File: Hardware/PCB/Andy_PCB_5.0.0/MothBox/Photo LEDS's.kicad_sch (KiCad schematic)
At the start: 48 parts, among them Q4 TJ10S04M3L,LXHQ, Q5 TJ10S04M3L,LXHQ, Q6 BC817, Q7 BC817

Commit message: made better camera
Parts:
- renumbered D1 to D10, D2 to D11, D3 to D12, D4 to D13, D5 to D14, D6 to D15, D7 to D16, D8 to D17, D9 to D18, D10 to D19, D11 to D20, D12 to D21, D13 to D22, D14 to D23, D15 to D24, D16 to D25, D17 to D26, D18 to D27, D19 to D28, D20 to D29, Q6 to Q4, Q4 to Q5, Q7 to Q6, Q5 to Q7, R55 to R51, R56 to R52, R57 to R53, R53 to R54, R58 to R55, R59 to R56, R51 to R57, R60 to R58, R61 to R59, R62 to R60, R63 to R61, R64 to R62, R65 to R63, R66 to R64, R67 to R65, R54 to R66, R68 to R67, R69 to R68, R52 to R69

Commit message: added female inverted header
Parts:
- removed D10, D11, D13, D14, D15, D16, D17, D18, D19, D20, D21, D22, D23, D24, D25, D26, D27, D28, D29: LED, LED_SMD:LED_Everlight-SMD3528_3.5x2.8mm_67-21ST, symbol Device:LED
- removed R52, R53, R55, R56, R58, R59, R60, R61, R62, R63, R64, R65, R67, R68, R70, R71, R72, R73, R74: 170R, Resistor_SMD:R_2512_6332Metric, symbol Device:R_US
- added LED1, LED10, LED11, LED13, LED14, LED15, LED16, LED17, LED18, LED19, LED2, LED20, LED21, LED22, LED23, LED24, LED25, LED26, LED27, LED28, LED29, LED3, LED34, LED35, LED36, LED37, LED38, LED39, LED4, LED40, LED41, LED42, LED43, LED44, LED45, LED46, LED47, LED48, LED49, LED5, LED50, LED51, LED52, LED6, LED7, LED8, LED9: XL-2835UWC-02, easyeda2kicad:LED-SMD_L3.5-W2.8-RD_1.25T-2PWT, symbol easyeda2kicad:XL-2835UWC-02
- added R10, R11, R12, R13, R14, R15, R2, R3, R52, R53, R55, R6, R7, R8, R9: FRC0805F30R0TS, easyeda2kicad:R0805, symbol easyeda2kicad:FRC0805F30R0TS
- LED12: renamed from D12; value LED -> XL-2835UWC-02; footprint LED_SMD:LED_Everlight-SMD3528_3.5x2.8mm_67-21ST -> easyeda2kicad:LED-SMD_L3.5-W2.8-RD_1.25T-2PWT; symbol Device:LED -> easyeda2kicad:XL-2835UWC-02; LCSC Part (none) -> C2843876
- R51: value 170R -> FRC0805F30R0TS; footprint Resistor_SMD:R_2512_6332Metric -> easyeda2kicad:R0805; symbol Device:R_US -> easyeda2kicad:FRC0805F30R0TS; LCSC Part (none) -> C2907256
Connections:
- net +12V_L_LED: now also R51.2, R2.2, R3.2, R53.2, R6.2, R7.2, R8.2, R9.2; no longer R51.1
- net +12V_R_LED: now also R10.2, R11.2, R12.2, R13.2, R14.2, R15.2, R52.2, R55.2
- net GND: now also LED11.1 (K), LED15.1 (K), LED18.1 (K), LED2.1 (K), LED22.1 (K), LED25.1 (K), LED28.1 (K), LED35.1 (K), LED37.1 (K), LED40.1 (K), LED43.1 (K), LED46.1 (K), LED49.1 (K), LED5.1 (K), LED52.1 (K), LED8.1 (K); no longer LED12.1 (K)
- net at LED12.2 (A): now also R51.1
- new net: LED6.2 (A), R3.1
- new net: LED16.1 (K), LED17.2 (A)
- new net: LED16.2 (A), R8.1
- new net: LED14.1 (K), LED15.2 (A)
- new net: LED23.2 (A), R11.1
- new net: LED42.1 (K), LED43.2 (A)
- new net: LED41.1 (K), LED42.2 (A)
- new net: LED45.1 (K), LED46.2 (A)
- new net: LED44.1 (K), LED45.2 (A)
- new net: LED9.2 (A), R6.1
- new net: LED7.1 (K), LED8.2 (A)
- new net: LED4.1 (K), LED5.2 (A)
- new net: LED21.1 (K), LED22.2 (A)
- new net: LED20.1 (K), LED21.2 (A)
- new net: LED19.2 (A), R9.1
- new net: LED48.1 (K), LED49.2 (A)
- new net: LED47.1 (K), LED48.2 (A)
- new net: LED29.1 (K), LED36.2 (A)
- new net: LED29.2 (A), R13.1
- new net: LED20.2 (A), R10.1
- new net: LED27.1 (K), LED28.2 (A)
- new net: LED34.1 (K), LED35.2 (A)
- new net: LED19.1 (K), LED34.2 (A)
- new net: LED50.1 (K), LED51.2 (A)
- new net: LED50.2 (A), R55.1
- new net: LED10.1 (K), LED11.2 (A)
- new net: LED10.2 (A), LED9.1 (K)
- new net: LED1.1 (K), LED2.2 (A)
- new net: LED1.2 (A), LED12.1 (K)
- new net: LED13.1 (K), LED14.2 (A)
- new net: LED13.2 (A), R7.1
- new net: LED36.1 (K), LED37.2 (A)
- new net: LED44.2 (A), R52.1
- new net: LED38.1 (K), LED39.2 (A)
- new net: LED38.2 (A), R14.1
- new net: LED39.1 (K), LED40.2 (A)
- new net: LED17.1 (K), LED18.2 (A)
- new net: LED26.1 (K), LED27.2 (A)
- new net: LED26.2 (A), R12.1
- new net: LED51.1 (K), LED52.2 (A)
- new net: LED3.1 (K), LED4.2 (A)
- new net: LED3.2 (A), R2.1
- new net: LED6.1 (K), LED7.2 (A)
- new net: LED41.2 (A), R15.1
- new net: LED23.1 (K), LED24.2 (A)
- new net: LED24.1 (K), LED25.2 (A)
- new net: LED47.2 (A), R53.1
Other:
- note added: "XINGLIGHT XL-2835UWC-02 60mA 6000K~7500K Yellow lens -20℃~+85℃ Positive Stick White 120° 200mW 3.4V SMD2835 LED Indication - Discrete ROH Figure out: How much current do these LEDs need how many batches per transistor thing what is the light angle of these LEDS (if any) without lens is cheaper Current per led = 60mA Total current = 8(columns) x 60mA = 480mA Total Luminous required = ?? lm Per led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"
- note removed: "Current per led = 55mA Total current = 10 x 55mA = 550mA Total Luminous required = 274 lm Per led luminous = 34 lm 10 led Luminous = 340 lm"

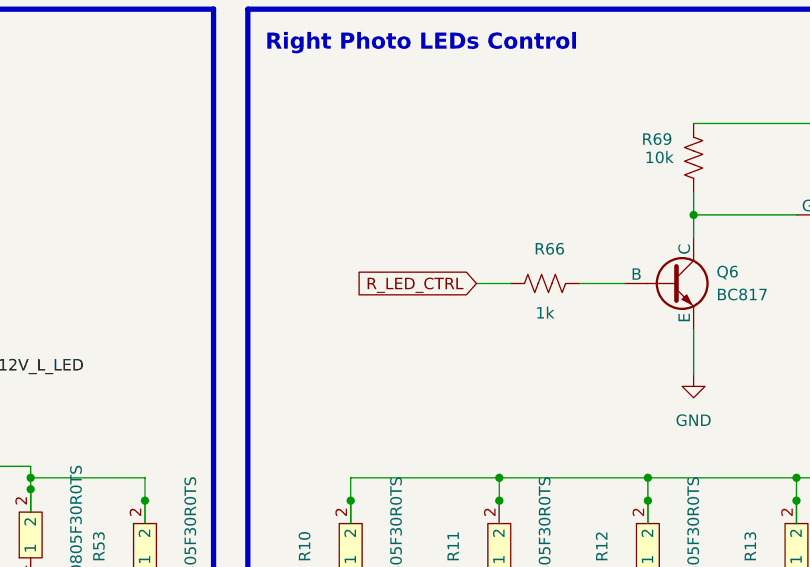
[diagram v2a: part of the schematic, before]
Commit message: Almost everything wired up
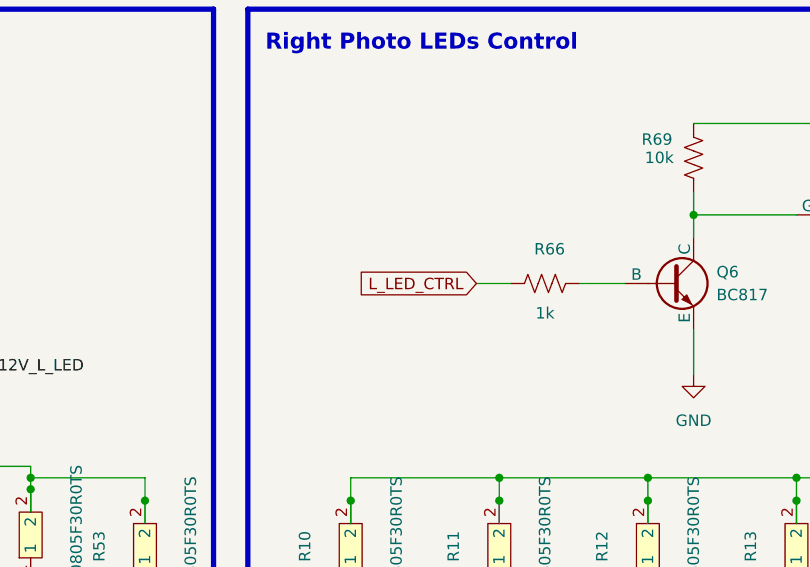
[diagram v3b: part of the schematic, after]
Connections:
- net R_LED_CTRL is gone; now on net L_LED_CTRL: R66.2
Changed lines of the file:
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@@
 		)
 	)
-	(global_label "R_LED_CTRL"
+	(global_label "L_LED_CTRL"
 		(shape input)
 		(at 179.07 66.04 180)
@@
 		)
 		(property "Intersheetrefs" "${INTERSHEET_REFS}"
-			(at 164.8968 66.04 0)
+			(at 165.1387 66.04 0)
 			(effects
 				(font

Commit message: omg pretty much all wired
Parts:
- added TP5: +12VLED L, TestPoint:TestPoint_THTPad_D1.0mm_Drill0.5mm, symbol Connector:TestPoint
- added TP6: +12VLED R, TestPoint:TestPoint_THTPad_D1.0mm_Drill0.5mm, symbol Connector:TestPoint
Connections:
- net +12V_L_LED: now also TP5.1
- net +12V_R_LED: now also TP6.1
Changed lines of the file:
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@@
 	)
 	(junction
+		(at 95.25 86.36)
+		(diameter 0)
+		(color 0 0 0 0)
+	)
+	(junction
 		(at 85.09 55.88)
 		(diameter 0)
@@
 		(color 0 0 0 0)
 	)
+	(junction
+		(at 223.52 87.63)
+		(diameter 0)
+		(color 0 0 0 0)
+	)
 	(wire
 		(pts
@@
 	(wire
 		(pts
+			(xy 223.52 87.63) (xy 229.87 87.63)
+		)
+		(stroke
+			(width 0)
+			(type default)
+		)
+	)
+	(wire
+		(pts
 			(xy 105.41 149.86) (xy 113.03 149.86)
 		)
@@
 	(wire
 		(pts
+			(xy 95.25 86.36) (xy 101.6 86.36)
+		)
+		(stroke
+			(width 0)
+			(type default)
+		)
+	)
+	(wire
+		(pts
 			(xy 139.7 128.27) (xy 139.7 129.54)
 		)
@@
 	(wire
 		(pts
-			(xy 86.36 86.36) (xy 101.6 86.36)
+			(xy 86.36 86.36) (xy 95.25 86.36)
 		)
 		(stroke
@@
 	(wire
 		(pts
-			(xy 214.63 87.63) (xy 229.87 87.63)
+			(xy 214.63 87.63) (xy 223.52 87.63)
 		)
 		(stroke
@@
 	)
 	(symbol
+		(lib_id "Connector:TestPoint")
+		(at 223.52 87.63 0)
+		(unit 1)
+		(exclude_from_sim no)
+		(in_bom yes)
+		(on_board yes)
+		(dnp no)
+		(property "Reference" "TP6"
+			(at 228.6 84.328 90)
+			(effects
+				(font
+					(size 1.27 1.27)
+				)
+			)
+		)
+		(property "Value" "+12VLED R"
+			(at 225.806 81.026 90)
+			(effects
+				(font
+					(size 1.27 1.27)
+				)
+			)
+		)
+		(property "Footprint" "TestPoint:TestPoint_THTPad_D1.0mm_Drill0.5mm"
+			(at 228.6 87.63 0)
+			(effects
+				(font
+					(size 1.27 1.27)
+				)
+				(hide yes)
+			)
+		)
+		(property "Datasheet" "~"
+			(at 228.6 87.63 0)
+			(effects
+				(font
+					(size 1.27 1.27)
+				)
+				(hide yes)
+			)
+		)
+		(property "Description" "test point"
+			(at 223.52 87.63 0)
+			(effects
+				(font
+					(size 1.27 1.27)
+				)
+				(hide yes)
+			)
+		)
+		(pin "1"
+		)
+		(instances
+			(project "MothBox"
+				(path "/9021e528-fc76-4423-a3f3-30f5652071cc/f4f29d93-7441-4557-92ff-295630596a60"
+					(reference "TP6")
+					(unit 1)
+				)
+			)
+		)
+	)
+	(symbol
 		(lib_id "easyeda2kicad:XL-2835UWC-02")
 		(at 127 134.62 90)
@@
 					(unit 1)
 				)
+			)
+		)
+	)
+	(symbol
+		(lib_id "Connector:TestPoint")
+		(at 95.25 86.36 0)
+		(unit 1)
+		(exclude_from_sim no)
+		(in_bom yes)
+		(on_board yes)
+		(dnp no)
+		(property "Reference" "TP5"
+			(at 100.33 83.058 90)
+			(effects
+				(font
+					(size 1.27 1.27)
+				)
+			)
+		)
+		(property "Value" "+12VLED L"
+			(at 97.536 79.756 90)
+			(effects
+				(font
+					(size 1.27 1.27)
+				)
+			)
+		)
+		(property "Footprint" "TestPoint:TestPoint_THTPad_D1.0mm_Drill0.5mm"
+			(at 100.33 86.36 0)
+			(effects
+				(font
+					(size 1.27 1.27)
+				)
+				(hide yes)
+			)
+		)
+		(property "Datasheet" "~"
+			(at 100.33 86.36 0)
+			(effects
+				(font
+					(size 1.27 1.27)
+				)
+				(hide yes)
+			)
+		)
+		(property "Description" "test point"
+			(at 95.25 86.36 0)
+			(effects
+				(font
+					(size 1.27 1.27)
+				)
+				(hide yes)
+			)
+		)
+		(pin "1"
+		)
+		(instances
+			(project "MothBox"
+				(path "/9021e528-fc76-4423-a3f3-30f5652071cc/f4f29d93-7441-4557-92ff-295630596a60"
+					(reference "TP5")
+					(unit 1)
+				)

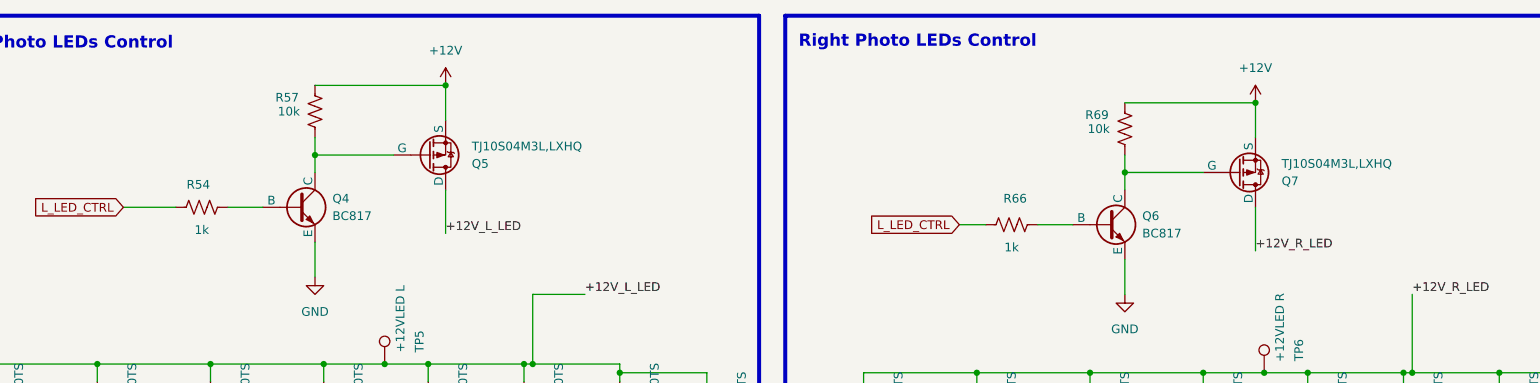
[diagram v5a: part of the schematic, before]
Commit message: Fixed parts with conflicting LCSC footprints
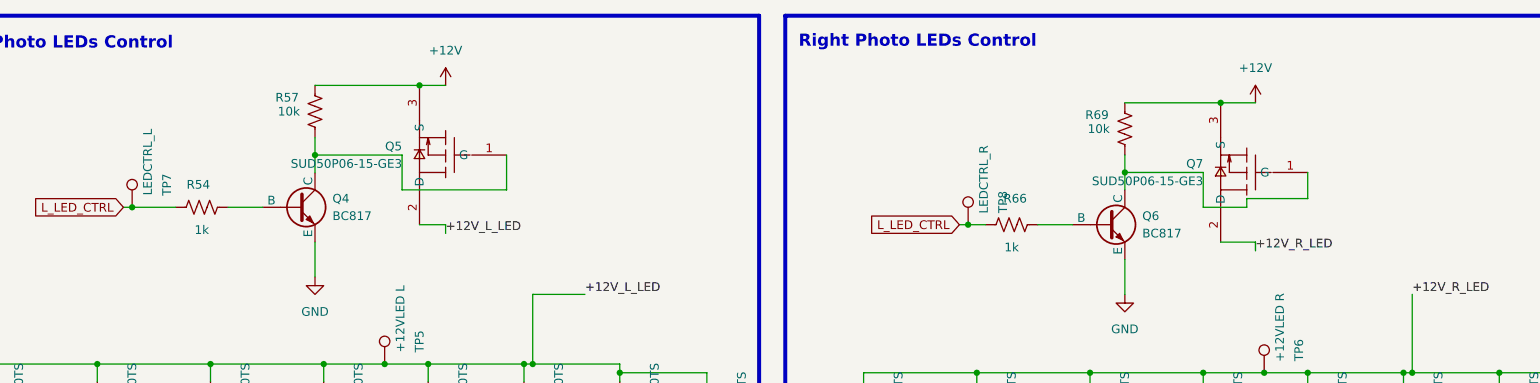
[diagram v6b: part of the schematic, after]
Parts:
- added TP7: LEDCTRL_L, TestPoint:TestPoint_THTPad_D1.0mm_Drill0.5mm, symbol Connector:TestPoint
- added TP8: LEDCTRL_R, TestPoint:TestPoint_THTPad_D1.0mm_Drill0.5mm, symbol Connector:TestPoint
- Q5, Q7: value TJ10S04M3L,LXHQ -> SUD50P06-15-GE3; footprint Package_TO_SOT_SMD:TO-252-2 -> easyeda2kicad:TO-252-3_L6.5-W5.8-P4.58-BL; symbol Simulation_SPICE:PMOS -> easyeda2kicad:SUD50P06-15-GE3; Digikey Part No TJ10S04M3L,LXHQ -> (none); LCSC Part (none) -> C141584; LCSC Part no  C41355200 -> (none)
- R10, R11, R12, R13, R14, R15, R2, R3, R51, R52, R53, R55, R6, R7, R8, R9: LCSC Part no  C2934094 -> (none)
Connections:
- net +12V_L_LED: now also Q5.2 (D); no longer Q5.1 (D)
- net +12V_R_LED: now also Q7.2 (D); no longer Q7.1 (D)
- net L_LED_CTRL: now also TP7.1, TP8.1
- net at Q6.3 (C), R69.1: now also Q7.1 (G); no longer Q7.2 (G)
- net at Q4.3 (C), R57.1: now also Q5.1 (G); no longer Q5.2 (G)
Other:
- moved on the sheet: Q5, Q7

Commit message: Maybe these files needed saving too for paul?
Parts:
- LED1, LED10, LED11, LED12, LED13, LED14, LED15, LED16, LED17, LED18, LED19, LED2, LED20, LED21, LED22, LED23, LED24, LED25, LED26, LED27, LED28, LED29, LED3, LED34, LED35, LED36, LED37, LED38, LED39, LED4, LED40, LED41, LED42, LED43, LED44, LED45, LED46, LED47, LED48, LED49, LED5, LED50, LED51, LED52, LED6, LED7, LED8, LED9: symbol easyeda2kicad:XL-2835UWC-02 -> MB_Library:XL-2835UWC-02
- Q4, Q6: symbol BC817:BC817_NPN_BJT -> MB_Library:BC817_NPN_BJT
- Q5, Q7: symbol easyeda2kicad:SUD50P06-15-GE3 -> MB_Library:SUD50P06-15-GE3
- R10, R11, R12, R13, R14, R15, R2, R3, R51, R52, R53, R55, R6, R7, R8, R9: symbol easyeda2kicad:FRC0805F30R0TS -> MB_Library:FRC0805F30R0TS
- R54, R57, R66, R69: symbol Device:R_US -> MB_Library:R_US
- TP5, TP6, TP7, TP8: symbol Connector:TestPoint -> MB_Library:TestPoint
